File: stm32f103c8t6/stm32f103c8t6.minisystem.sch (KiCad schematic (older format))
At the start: 1 part

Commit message: 发现 kicad 本身已经提供了stm32 器件库。
¨@#
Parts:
- removed U?: STM32F103C8T6, symbol STM32F103C8T6
- added U?: STM32F100C8, LQFP48, symbol STM32F100C8
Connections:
- net labels removed: VBAT
- wire segments 1 -> 0
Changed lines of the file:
@@
-EESchema Schematic File Version 2  date 2015年08月14日 星期五 13时09分35秒
+EESchema Schematic File Version 2
 LIBS:power
 LIBS:device
@@
 LIBS:valves
 LIBS:stm32
-EELAYER 25  0
+LIBS:stm32f103c8t6.minisystem-cache
+EELAYER 27 0
 EELAYER END
-$Descr A4 11700 8267
+$Descr A4 11693 8268
 encoding utf-8
 Sheet 1 1
@@
 Date "14 aug 2015"
 Rev "001"
-Comp "JNCompany Ltd."
+Comp "an6734"
 Comment1 "Author: an6734@yahoo.com"
 Comment2 ""
@@
 Comment4 ""
 $EndDescr
-Text Label 750  2500 0    60   ~ 0
-VBAT
-Wire Wire Line
-	550  2500 1100 2500
 $Comp
-L STM32F103C8T6 U?
-U 1 1 55CD75FF
-P 2600 3150
-F 0 "U?" H 3100 2100 60  0000 C CNN
-F 1 "STM32F103C8T6" H 3400 2000 60  0000 C CNN
-	1    2600 3150
+L STM32F100C8 U?
+U 1 1 55CDB53A
+P 2750 2850
+F 0 "U?" H 1450 4500 60  0000 C CNN
+F 1 "STM32F100C8" H 3800 1200 60  0000 C CNN
+F 2 "LQFP48" H 2750 2850 40  0000 C CIN
+F 3 "" H 2750 2850 60  0000 C CNN
+	1    2750 2850
 	1    0    0    -1
 $EndComp

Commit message: 继续原理图输入。
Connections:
- net VBAT: now reaches U?.1 (VBAT)
- net PA0: now reaches U?.10 (WKUP/USART2_CTS/ADC1_IN0/TIM2_CH1_ETR/PA0)
- net PA1: now reaches U?.11 (USART2_RTS/ADC1_IN1/TIM2_CH2/PA1)
- net PA2: now reaches U?.12 (USART2_TX/ADC1_IN2/TIM2_CH3/TIM15_CH1/PA2)
- net PA3: now reaches U?.13 (USART2_RX/ADC1_IN3/TIM2_CH4/TIM15_CH2/PA3)
- net PA4: now reaches U?.14 (SPI1_NSS/ADC1_IN4/USART2_CK/DAC1_OUT/PA4)
- net PA5: now reaches U?.15 (SPI1_SCK/ADC1_IN5/DAC2_OUT/PA5)
- net PA6: now reaches U?.16 (SPI1_MISO/ADC1_IN6/TIM3_CH1/PA6)
- net PA7: now reaches U?.17 (SPI1_MOSI/ADC1_IN7/TIM3_CH2/PA7)
- net PB0: now reaches U?.18 (PB0/ADC1_IN8/TIM3_CH3)
- net PB1: now reaches U?.19 (PB1/ADC1_IN9/TIM3_CH4)
- net PC13: now reaches U?.2 (PC13/TAMPER_RTC)
- net BOOT1: now reaches U?.20 (PB2/BOOT1)
- net PB10: now reaches U?.21 (PB10/I2C2_SCL/USART3_TX)
- net PB11: now reaches U?.22 (PB11/I2C2_SDA/USART3_RX)
- net GND: now reaches U?.23 (VSS)
- net GND: now also U?.35 (VSS), U?.47 (VSS), U?.8 (VSSA)
- net 3.3V: now reaches U?.24 (VDD)
- net 3.3V: now also U?.36 (VDD), U?.48 (VDD)
- net PB12: now reaches U?.25 (PB12/SPI2_NSS/I2C2_SMBA/TIM1_BKIN/USART3_CK)
- net PB13: now reaches U?.26 (PB13/SPI2_SCK/TIM1_CH1N/USART3_CTS)
- net PB14: now reaches U?.27 (PB14/SPI2_MISO/TIM1_CH2N/USART3_RTS)
- net PB15: now reaches U?.28 (PB15/SPI2_MOSI/TIM1_CH3N/TIM15_CH1N)
- net PA8: now reaches U?.29 (USART1_CK/MCO/TIM1_CH1/PA8)
- net OSC32_IN: now reaches U?.3 (PC14/OSC32_IN)
- net U1_TX: now reaches U?.30 (USART1_TX/TIM1_CH2/TIM15_BKIN/PA9)
- net U1_RX: now reaches U?.31 (USART1_RX/TIM1_CH3/TIM17_BKIN/PA10)
- net USB_DM: now reaches U?.32 (USART1_CTS/TIM1_CH4/PA11)
- net USB_DP: now reaches U?.33 (USART1_RTS/TIM1_ETR/PA12)
- net JTAG_TMS: now reaches U?.34 (JTMS/SWDIO/PA13)
- net JTAG_TCK: now reaches U?.37 (JTCK/SWCLK/PA14)
- net JTAG_TDI: now reaches U?.38 (JTDI/PA15)
- net JTAG_TDO: now reaches U?.39 (PB3/JTDO)
- net OSC32_OUT: now reaches U?.4 (PC15/OSC32_OUT)
- net JTAG_NTRST: now reaches U?.40 (PB4/NJRST)
- net PB5: now reaches U?.41 (PB5/I2C1_SMBA/TIM16_BKIN)
- net PB6: now reaches U?.42 (PB6/I2C1_SCL/TIM4_CH1/TIM16_CH1N)
- net PB7: now reaches U?.43 (PB7/I2C1_SDA/TIM17_CH1N/TIM4_CH2)
- net BOOT0: now reaches U?.44 (BOOT0)
- net PB8: now reaches U?.45 (PB8/TIM4_CH3/TIM16_CH1/CEC)
- net PB9: now reaches U?.46 (PB9/TIM4_CH4/TIM17_CH1)
- net OSC_IN: now reaches U?.5 (OSC_IN)
- net OSC_OUT: now reaches U?.6 (OSC_OUT)
- net NRST: now reaches U?.7 (~NRST)
- net VDDA: now reaches U?.9 (VDDA)
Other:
- moved on the sheet: U?
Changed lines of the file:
@@
 L STM32F100C8 U?
 U 1 1 55CDB53A
-P 2750 2850
-F 0 "U?" H 1450 4500 60  0000 C CNN
-F 1 "STM32F100C8" H 3800 1200 60  0000 C CNN
-F 2 "LQFP48" H 2750 2850 40  0000 C CIN
-F 3 "" H 2750 2850 60  0000 C CNN
-	1    2750 2850
+P 3400 3700
+F 0 "U?" H 2100 5350 60  0000 C CNN
+F 1 "STM32F100C8" H 4450 2050 60  0000 C CNN
+F 2 "LQFP48" H 3400 3700 40  0000 C CIN
+F 3 "" H 3400 3700 60  0000 C CNN
+	1    3400 3700
 	1    0    0    -1
 $EndComp
+Text GLabel 1150 3300 0    50   Input ~ 0
+OSC32_IN
+Text GLabel 1150 3400 0    50   Input ~ 0
+OSC32_OUT
+Wire Wire Line
+	1150 3300 1900 3300
+Wire Wire Line
+	1900 3400 1150 3400
+Text GLabel 1150 2650 0    50   Input ~ 0
+OSC_IN
+Text GLabel 1150 2800 0    50   Input ~ 0
+OSC_OUT
+Wire Wire Line
+	1900 2650 1150 2650
+Wire Wire Line
+	1900 2800 1150 2800
+Text GLabel 1150 2300 0    50   Input ~ 0
+NRST
+Text GLabel 1150 2450 0    50   Input ~ 0
+BOOT0
+Text GLabel 1150 3750 0    50   Input ~ 0
+BOOT1
+Text GLabel 1150 3950 0    50   Input ~ 0
+JTAG_NTRST
+Text GLabel 1150 3000 0    50   Input ~ 0
+VBAT
+Text GLabel 950  3550 0    50   Input ~ 0
+PB0
+Text GLabel 950  3650 0    50   Input ~ 0
+PB1
+Text GLabel 1150 3850 0    50   Input ~ 0
+JTAG_TDO
+Text GLabel 950  4050 0    50   Input ~ 0
+PB5
+Text GLabel 950  4150 0    50   Input ~ 0
+PB6
+Text GLabel 950  4250 0    50   Input ~ 0
+PB7
+Text GLabel 950  4350 0    50   Input ~ 0
+PB8
+Text GLabel 950  4450 0    50   Input ~ 0
+PB9
+Text GLabel 950  4550 0    50   Input ~ 0
+PB10
+Text GLabel 950  4650 0    50   Input ~ 0
+PB11
+Text GLabel 950  4750 0    50   Input ~ 0
+PB12
+Text GLabel 950  4850 0    50   Input ~ 0
+PB13
+Text GLabel 950  4950 0    50   Input ~ 0
+PB14
+Text GLabel 950  5050 0    50   Input ~ 0
+PB15
+Wire Wire Line
+	1900 3000 1150 3000
+Wire Wire Line
+	1900 3550 950  3550
+Wire Wire Line
+	1900 3650 950  3650
+Wire Wire Line
+	1900 3750 1150 3750
+Wire Wire Line
+	1900 3850 1150 3850
+Wire Wire Line
+	1900 3950 1150 3950
+Wire Wire Line
+	1900 4050 950  4050
+Wire Wire Line
+	1900 4150 950  4150
+Wire Wire Line
+	1900 4250 950  4250
+Wire Wire Line
+	1900 4350 950  4350
+Wire Wire Line
+	1900 4450 950  4450
+Wire Wire Line
+	1900 4550 950  4550
+Wire Wire Line
+	1900 4650 950  4650
+Wire Wire Line
+	1900 4750 950  4750
+Wire Wire Line
+	1900 4850 950  4850
+Wire Wire Line
+	1900 4950 950  4950
+Wire Wire Line
+	1900 5050 950  5050
+Wire Wire Line
+	1900 2450 1150 2450
+Wire Wire Line
+	1900 2300 1150 2300
+Text GLabel 950  3200 0    50   Input ~ 0
+PC13
+Wire Wire Line
+	1900 3200 950  3200
+Text GLabel 2250 1800 0    50   Input ~ 0
+3.3V
+Text GLabel 2250 5600 0    50   Input ~ 0
+GND
+Wire Wire Line
+	3100 5450 3100 5600
+Wire Wire Line
+	3700 5450 3700 5600
+Wire Wire Line
+	3400 5450 3400 5600
+Wire Wire Line
+	3250 5450 3250 5600
+Wire Wire Line
+	3700 5600 2250 5600
+Connection ~ 3400 5600
+Connection ~ 3250 5600
+Connection ~ 3100 5600
+Wire Wire Line
+	3400 1950 3400 1800
+Wire Wire Line
+	3250 1950 3250 1800
+Wire Wire Line
+	3100 1950 3100 1800
+Wire Wire Line
+	3400 1800 2250 1800
+Connection ~ 3250 1800
+Connection ~ 3100 1800
+Text GLabel 2250 1650 0    50   Input ~ 0
+VDDA
+Wire Wire Line
+	3700 1950 3700 1650
+Wire Wire Line
+	3700 1650 2250 1650
+Wire Wire Line
+	4900 3350 5400 3350
+Wire Wire Line
+	4900 3450 5400 3450
+Text GLabel 5400 3350 2    50   Input ~ 0
+U1_TX
+Text GLabel 5400 3450 2    50   Input ~ 0
+U1_RX
+Text GLabel 5400 3550 2    50   Input ~ 0
+USB_DM
+Text GLabel 5400 3650 2    50   Input ~ 0
+USB_DP
+Text GLabel 5400 3750 2    50   Input ~ 0
+JTAG_TMS
+Text GLabel 5400 3850 2    50   Input ~ 0
+JTAG_TCK
+Text GLabel 5400 3950 2    50   Input ~ 0
+JTAG_TDI
+Text GLabel 5600 2450 2    50   Input ~ 0
+PA0
+Text GLabel 5600 2550 2    50   Input ~ 0
+PA1
+Text GLabel 5600 2650 2    50   Input ~ 0
+PA2
+Text GLabel 5600 2750 2    50   Input ~ 0
+PA3
+Text GLabel 5600 2850 2    50   Input ~ 0
+PA4
+Text GLabel 5600 2950 2    50   Input ~ 0
+PA5
+Text GLabel 5600 3050 2    50   Input ~ 0
+PA6
+Text GLabel 5600 3150 2    50   Input ~ 0
+PA7
+Text GLabel 5600 3250 2    50   Input ~ 0
+PA8
+Wire Wire Line
+	4900 2450 5600 2450
+Wire Wire Line
+	4900 2550 5600 2550
+Wire Wire Line
+	4900 2650 5600 2650
+Wire Wire Line
+	4900 2750 5600 2750
+Wire Wire Line
+	4900 2850 5600 2850
+Wire Wire Line
+	4900 2950 5600 2950
+Wire Wire Line
+	4900 3050 5600 3050
+Wire Wire Line
+	4900 3150 5600 3150
+Wire Wire Line
+	4900 3250 5600 3250
+Wire Wire Line
+	4900 3550 5400 3550
+Wire Wire Line
+	4900 3650 5400 3650
+Wire Wire Line
+	4900 3750 5400 3750
+Wire Wire Line
+	4900 3850 5400 3850
+Wire Wire Line
+	4900 3950 5400 3950
 $EndSCHEMATC

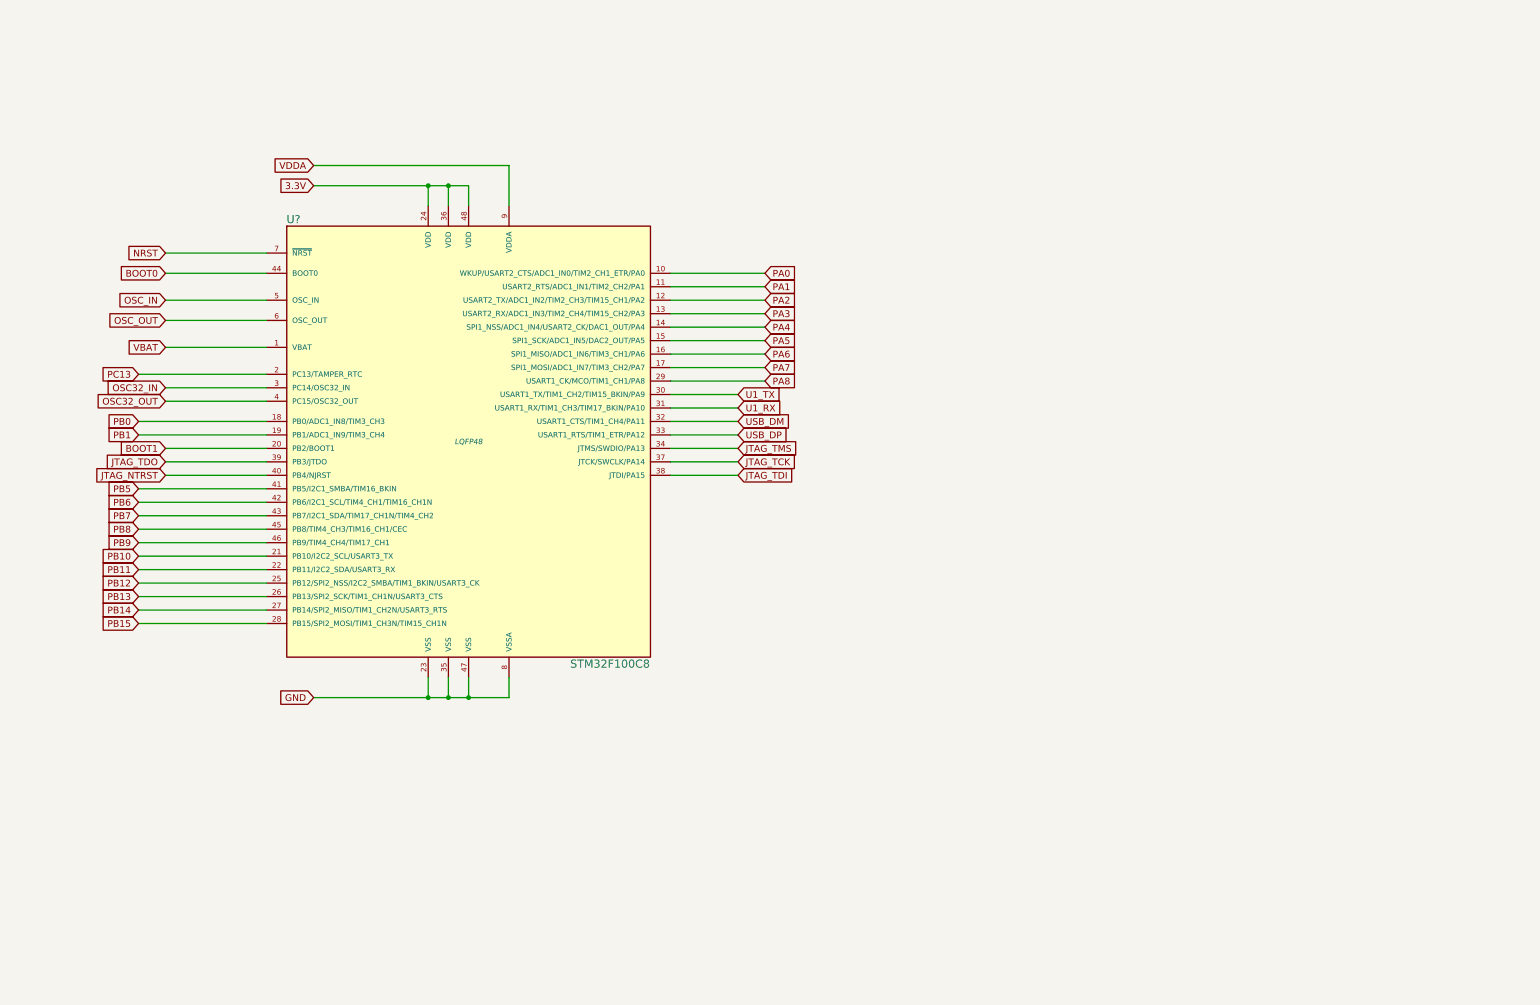
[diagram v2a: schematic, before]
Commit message: 继续完成电路原理图。尚缺AMS1117-3.3这个器件没画。
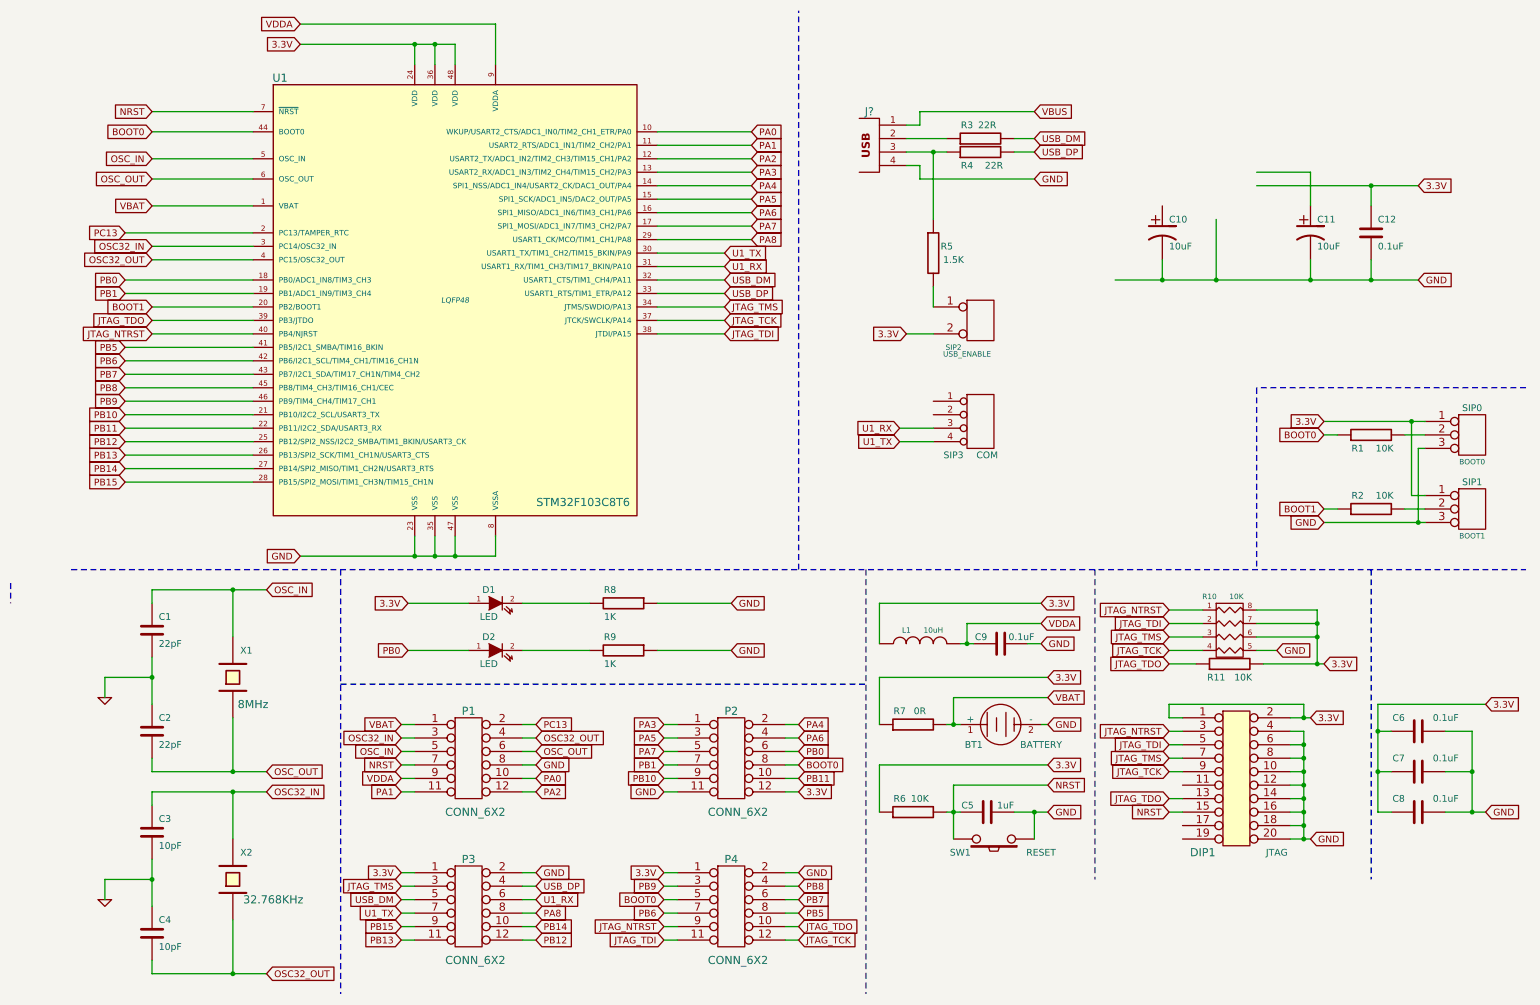
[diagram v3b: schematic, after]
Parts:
- added 1.5K: R5, symbol R
- added BT1: BATTERY, symbol BATTERY
- added C1, C2: 22pF, symbol C
- added C10, C11: 10uF, symbol CP1
- added C12, C6, C7, C8, C9: 0.1uF, symbol C
- added C3, C4: 10pF, symbol C
- added C5: 1uF, symbol C
- added D1, D2: LED, symbol LED
- added DIP1: JTAG, symbol CONN_10X2
- added J?: USB_2, symbol USB_2
- added L1: 10uH, symbol INDUCTOR
- added P1, P2, P3, P4: CONN_6X2, symbol CONN_6X2
- added R1, R11, R2, R6: 10K, symbol R
- added R10: 10K, symbol R_PACK4
- added R3, R4: 22R, symbol R
- added R7: 0R, symbol R
- added R8, R9: 1K, symbol R
- added SIP0: BOOT0, symbol CONN_3
- added SIP1: BOOT1, symbol CONN_3
- added SIP2: USB_ENABLE, symbol CONN_2
- added SIP3: COM, symbol CONN_4
- added SW1: RESET, symbol SW_PUSH
- added X1: 8MHz, symbol CRYSTAL
- added X2: 32.768KHz, symbol CRYSTAL
- U1: renamed from U?; value STM32F100C8 -> STM32F103C8T6
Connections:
- net 3.3V: now also C12.1, C6.1, C7.1, C8.1, D1.1 (A), DIP1.1 (P1), DIP1.2 (P2), L1.1, P2.12, P3.1 (P1), P4.1 (P1), R10.6 (R3), R10.7 (R2), R10.8 (R1), R11.2, R6.1, R7.1, SIP0.1 (P1), SIP1.1 (P1), SIP2.2 (PM)
- net BOOT0: now also P2.8 (P8), P4.5 (P5), R1.1
- net BOOT1: now also R2.1
- net GND: now also BT1.2 (-), C1.2, C10.2, C11.2, C12.2, C2.1, C3.2, C4.1, C5.2, C6.2, C7.2, C8.2, C9.2, DIP1.10 (P10), DIP1.12 (P12), DIP1.14 (P14), DIP1.16 (P16), DIP1.18 (P18), DIP1.20 (P20), DIP1.4 (P4), DIP1.6 (P6), DIP1.8 (P8), J?.4, P1.8 (P8), P2.11, P3.2 (P2), P4.2 (P2), R10.5 (R4), R8.1, R9.1, SIP0.3 (P3), SIP1.3 (P3), SW1.1
- net JTAG_NTRST: now also DIP1.3 (P3), P4.9, R10.1 (P1)
- net JTAG_TCK: now also DIP1.9 (P9), P4.12, R10.4 (P4)
- net JTAG_TDI: now also DIP1.5 (P5), P4.11, R10.2 (P2)
- net JTAG_TDO: now also DIP1.13 (P13), P4.10, R11.1
- net JTAG_TMS: now also DIP1.7 (P7), P3.3 (P3), R10.3 (P3)
- net NRST: now also C5.1, DIP1.15 (P15), P1.7 (P7), R6.2, SW1.2
- net OSC32_IN: now also C3.1, P1.3 (P3), X2.2
- net OSC32_OUT: now also C4.2, P1.4 (P4), X2.1
- net OSC_IN: now also C1.1, P1.5 (P5), X1.2
- net OSC_OUT: now also C2.2, P1.6 (P6), X1.1
- net PA0: now also P1.10
- net PA1: now also P1.11
- net PA2: now also P1.12
- net PA3: now also P2.1 (P1)
- net PA4: now also P2.2 (P2)
- net PA5: now also P2.3 (P3)
- net PA6: now also P2.4 (P4)
- net PA7: now also P2.5 (P5)
- net PA8: now also P3.8 (P8)
- net PB0: now also D2.1 (A), P2.6 (P6)
- net PB1: now also P2.7 (P7)
- net PB10: now also P2.9
- net PB11: now also P2.10
- net PB12: now also P3.12
- net PB13: now also P3.11
- net PB14: now also P3.10
- net PB15: now also P3.9
- net PB5: now also P4.8 (P8)
- net PB6: now also P4.7 (P7)
- net PB7: now also P4.6 (P6)
- net PB8: now also P4.4 (P4)
- net PB9: now also P4.3 (P3)
- net PC13: now also P1.2 (P2)
- net U1_RX: now also P3.6 (P6), SIP3.3 (P3)
- net U1_TX: now also P3.7 (P7), SIP3.4 (P4)
- net USB_DM: now also P3.5 (P5), R3.2
- net USB_DP: now also P3.4 (P4), R4.2
- net VBAT: now also BT1.1 (+), P1.1 (P1), R7.2
- net VDDA: now also C9.1, L1.2, P1.9
- new net: D2.2 (K), R9.2
- new net: D1.2 (K), R8.2
- new net: J?.2, R3.1
- new net: 1.5K.1, J?.3, R4.1
- new net: 1.5K.2, SIP2.1 (P1)
- new net: R1.2, SIP0.2 (PM)
- new net: R2.2, SIP1.2 (PM)
- new net VBUS: J?.1
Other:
- moved on the sheet: U1

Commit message: 继续修改原理图。
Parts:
- removed J?: USB_2, symbol USB_2
- added USB1: USB-MINI-B, symbol USB-MINI-B
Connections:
- net GND: now also SIP3.2 (P2), USB1.5 (GND), USB1.6 (SHELL1)
- net VBUS: now also SIP3.1 (P1), USB1.1 (VBUS)
- net at R3.1: now also USB1.2 (D-)
- net at 1.5K.1, R4.1: now also USB1.3 (D+)
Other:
- moved on the sheet: 1.5K, C10, C11, C12, R3, R4, SIP2, SIP3

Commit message: 原理图完成。
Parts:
- added U2: AMS1117-3.3, SOT-223, symbol LT1129CST-3.3
- R5: renamed from 1.5K; value R5 -> 1.5K
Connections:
- net 3.3V: now also C11.1, U2.3 (OUT)
- net GND: now also U2.2 (GND)
- net VBUS: now also C10.1, U2.1 (VIN)
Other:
- moved on the sheet: C10, C11, C12, R1, R2, R3, R4, R5, SIP0, SIP1, SIP2, SIP3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
